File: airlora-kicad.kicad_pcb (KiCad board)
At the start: 4 copper layers, 77 x 77 mm, 185 parts, among them IC1 BALFHB-WL-02D3, J1 12V, J10 I2C, J11 UART2, J12 UART_MAIN, J2 Conn_Coaxial, J3 Led, J4 SHT, J5 I2C, J6 A_NO2, J7 UART1, J8 A_CO, J9 I2C, Q1 S8050, Q2 S8050, Q3 S8050, Q4 S8050, Q5 S8050, Q6 S8050, Q7 S8050, Q8 S8050, Q9 S8050, SW1 SW_Push, SW2 SW_Slide_DPDT, SW3 SW_Push, U1 TPS7A2633DRVR, U2 TPS54202DDC, U3 TPS7A2633DRVR, U4 BGS12WN6E6327, U5 STM32WLE5CCUx, U6 STM32F103C8Tx, X1 32MHZ, Y1 32.768kHz, Y2 8Mhz

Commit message: Update PCB layout
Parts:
- removed C10, C9: 1uF, Capacitor_SMD:C_0805_2012Metric
- removed C42: 4.7uF, Capacitor_SMD:C_0603_1608Metric
- removed C43, C44, C45, C46, C47: 100nf, Capacitor_SMD:C_0402_1005Metric
- removed C48, C49: 22PF, Capacitor_SMD:C_0402_1005Metric
- removed C50: 100nF, Capacitor_SMD:C_0402_1005Metric
- removed D4: LED, LED_SMD:LED_0603_1608Metric_Pad1.05x0.95mm_HandSolder
- removed J6: A_NO2, Connector_JST:JST_XH_B3B-XH-A_1x03_P2.50mm_Vertical
- removed J8: A_CO, Connector_JST:JST_XH_B3B-XH-A_1x03_P2.50mm_Vertical
- removed Q5, Q7: S8050, Package_TO_SOT_SMD:SOT-23
- removed R28, R29: 10k, Resistor_SMD:R_0402_1005Metric
- removed SW2: SW_Slide_DPDT, Button_Switch_THT:SW_E-Switch_EG1271_SPDT
- removed SW3: SW_Push, Button_Switch_SMD:SW_Tactile_SPST_NO_Straight_CK_PTS636Sx25SMTRLFS
- removed U3: TPS7A2633DRVR, footprint:TPS7A2633DRVR
- removed U6: STM32F103C8Tx, Package_QFP:LQFP-48_7x7mm_P0.5mm
- removed X1: 32MHZ, footprint:NX2016SA_NDK
- removed Y2: 8Mhz, Crystal:Crystal_SMD_3225-4Pin_3.2x2.5mm
- removed kibuzzard-667528BC: G***, kibuzzard-667528BC
- removed kibuzzard-667528D4: G***, kibuzzard-667528D4
- removed the kibuzzard-66752922 at (124.1, 87.6)
- removed the kibuzzard-66752922 at (123.9, 76.0)
- removed the kibuzzard-667540EB at (124.1, 85.1)
- removed the kibuzzard-667540EB at (123.9, 73.6)
- removed kibuzzard-66754104: G***, kibuzzard-66754104
- removed the kibuzzard-66754176 at (96.7, 89.6)
- removed kibuzzard-667541E6 (x4): G***, kibuzzard-667541E6
- removed kibuzzard-667541EF (x4): G***, kibuzzard-667541EF
- removed kibuzzard-66754524: G***, kibuzzard-66754524
- removed the kibuzzard-66763ACD at (81.7, 87.9)
- removed kibuzzard-668CA440: G***, kibuzzard-668CA440
- removed kibuzzard-668CA458: G***, kibuzzard-668CA458
- removed kibuzzard-668CA46A: G***, kibuzzard-668CA46A
- removed kibuzzard-668CA479: G***, kibuzzard-668CA479
- removed kibuzzard-668CA498: G***, kibuzzard-668CA498
- removed kibuzzard-668CA4A7: G***, kibuzzard-668CA4A7
- removed kibuzzard-668CA4B6: G***, kibuzzard-668CA4B6
- removed kibuzzard-668CA4DF: G***, kibuzzard-668CA4DF
- removed kibuzzard-668CA658: G***, kibuzzard-668CA658
- removed kibuzzard-668CA679: G***, kibuzzard-668CA679
- removed kibuzzard-668F38B2: G***, kibuzzard-668F38B2
- removed kibuzzard-6690D059: G***, kibuzzard-6690D059
- removed kibuzzard-6690D084: G***, kibuzzard-6690D084
- removed kibuzzard-6690D099: G***, kibuzzard-6690D099
- added J13: UART_MAIN, Connector_JST:JST_XH_B3B-XH-A_1x03_P2.50mm_Vertical, F.Cu at (183.6, 86.8)
- added J14: Conn_01x02_Pin, Connector_PinHeader_2.54mm:PinHeader_1x02_P2.54mm_Vertical, F.Cu at (129.7, 96.8)
- added J15: Conn_01x02_Pin, Connector_PinHeader_2.54mm:PinHeader_1x02_P2.54mm_Vertical, F.Cu at (142.8, 90.9)
- added L6: 1400R@1GHz, Inductor_SMD:L_0402_1005Metric, F.Cu at (172.4, 103.3)
- added TP1: TestPoint, TestPoint:TestPoint_Loop_D1.80mm_Drill1.0mm_Beaded, F.Cu at (134.5, 76.2)
- added TP2: TestPoint, TestPoint:TestPoint_Loop_D1.80mm_Drill1.0mm_Beaded, F.Cu at (138.6, 76.2)
- added TP3: TestPoint, TestPoint:TestPoint_Loop_D1.80mm_Drill1.0mm_Beaded, F.Cu at (149.0, 103.8)
- added TP4: TestPoint, TestPoint:TestPoint_Loop_D1.80mm_Drill1.0mm_Beaded, F.Cu at (144.2, 103.8)
- added TP5: TestPoint, TestPoint:TestPoint_Loop_D1.80mm_Drill1.0mm_Beaded, F.Cu at (165.6, 80.7)
- added TP6: TestPoint, TestPoint:TestPoint_Loop_D1.80mm_Drill1.0mm_Beaded, F.Cu at (169.9, 80.7)
- added XTAL1: NT2016SA-32M-END4263A, footprint:NT2016SA-32M-END4263A_NDK, F.Cu at (171.8, 105.9)
- added kibuzzard-66752922: G***, kibuzzard-66752922, F.Cu at (175.7, 92.1)
- added kibuzzard-66A47256: G***, kibuzzard-66A47256, F.Cu at (122.2, 115.1)
- added kibuzzard-66A70081: G***, kibuzzard-66A70081, B.Cu at (145.7, 63.9)
- added kibuzzard-66A7008A: G***, kibuzzard-66A7008A, B.Cu at (147.7, 63.9)
- added kibuzzard-66A70091: G***, kibuzzard-66A70091, B.Cu at (159.5, 64.0)
- added kibuzzard-66A70098: G***, kibuzzard-66A70098, B.Cu at (161.4, 64.0)
- added kibuzzard-66A700A1: G***, kibuzzard-66A700A1, B.Cu at (173.2, 64.1)
- added kibuzzard-66A704F7: G***, kibuzzard-66A704F7, B.Cu at (175.2, 64.1)
- added kibuzzard-66A704FE: G***, kibuzzard-66A704FE, F.Cu at (170.5, 84.8)
- added kibuzzard-66A704FE: G***, kibuzzard-66A704FE, B.Cu at (179.6, 75.3)
- added kibuzzard-66A70504: G***, kibuzzard-66A70504, F.Cu at (165.2, 84.8)
- added kibuzzard-66A70504: G***, kibuzzard-66A70504, B.Cu at (179.6, 72.8)
- added kibuzzard-66A7052C: G***, kibuzzard-66A7052C, F.Cu at (132.4, 80.3)
- added kibuzzard-66A70534: G***, kibuzzard-66A70534, F.Cu at (140.5, 80.3)
- added kibuzzard-66A705CB: G***, kibuzzard-66A705CB, F.Cu at (149.4, 108.3)
- added kibuzzard-66A705D3: G***, kibuzzard-66A705D3, F.Cu at (144.1, 108.3)
- added kibuzzard-66A7121E: G***, kibuzzard-66A7121E, F.Cu at (175.7, 86.9)
- added kibuzzard-66A71226: G***, kibuzzard-66A71226, F.Cu at (175.7, 89.5)
- added kibuzzard-66A7130C: G***, kibuzzard-66A7130C, F.Cu at (146.5, 113.3)
- added kibuzzard-66A71314: G***, kibuzzard-66A71314, F.Cu at (151.3, 113.3)
- added kibuzzard-66A71938: G***, kibuzzard-66A71938, F.Cu at (148.3, 75.3)
- C3: footprint Capacitor_SMD:C_0402_1005Metric -> Capacitor_SMD:C_0603_1608Metric
- C37, C41: value 6.8pF -> 10pF
- J11: value UART2 -> Conn_01x02_Pin; footprint Connector_JST:JST_XH_B4B-XH-A_1x04_P2.50mm_Vertical -> Connector_PinHeader_2.54mm:PinHeader_1x02_P2.54mm_Vertical
- J12: value UART_MAIN -> STlink; footprint Connector_JST:JST_XH_B4B-XH-A_1x04_P2.50mm_Vertical -> Connector_JST:JST_XH_B5B-XH-A_1x05_P2.50mm_Vertical
- R10: value 10K -> 220
- R11: value 1.96M -> 3k
- R12: value 1.18M -> 1K; footprint Resistor_SMD:R_0402_1005Metric -> Resistor_SMD:R_0603_1608Metric
- R13: value 1k -> 1K; footprint Resistor_SMD:R_0402_1005Metric -> Resistor_SMD:R_0603_1608Metric
- R16, R22, R24: value 1K -> 4.7K
- R27: value 1k -> 4.7K
- moved J12 119.0 mm to (183.6, 100.2)
- moved kibuzzard-6690D08F 107.0 mm to (176.9, 110.4)
- moved R10 91.3 mm to (169.5, 104.5)
- moved R12 76.9 mm to (151.5, 122.3)
- moved R13 70.6 mm to (146.4, 122.3)
- moved R27 70.4 mm to (149.1, 101.3), turned to 0 degrees
- moved C33 69.6 mm to (165.8, 93.6), turned to 180 degrees
- moved C36 68.2 mm to (163.9, 93.6), turned to 180 degrees
- moved C6 68.0 mm to (135.4, 88.5)
- moved U1 68.0 mm to (135.4, 91.2)
- moved C1 68.0 mm to (135.6, 93.8)
- moved R2 68.0 mm to (131.4, 92.0)
- moved R3 68.0 mm to (131.4, 90.5)
- moved R4 68.0 mm to (131.4, 89.0)
- moved Y1 67.1 mm to (164.8, 95.0), turned to 0 degrees
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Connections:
- C29 pad 2: /AirLora V3/MCU/RFO_LP -> /AirLora V3/MCU/RFO_HP
- C37 pad 1: GND -> Net-(XTAL1-VCC)
- C37 pad 2: Net-(U5-OSC_IN) -> GND
- C41 pad 1: Net-(U5-OSC_OUT) -> /AirLora V3/MCU/XTA
- C41 pad 2: GND -> Net-(C41-Pad2)
- C6 pad 1: +3.3V_HP -> Net-(J15-Pin_1)
- C7 pad 1: +5V -> a
- C8 pad 1: +5V -> a
- D1 pad 2: +3.3V_HP -> +3.3V
- D3 pad 2: +3.3V -> +12V
- J1 pad 1: +12V -> Net-(J1-Pin_1)
- J10 pad 3: /AirLora V3/MCU Sub/SCL1 -> /AirLora V3/MCU/SCL2
- J10 pad 4: /AirLora V3/MCU Sub/SDA1 -> /AirLora V3/MCU/SDA2
- J11 pad 1: GND -> Net-(J1-Pin_1)
- J11 pad 2: +3.3V -> +12V
- J12 pad 1: /AirLora V3/MCU/UART1_RX -> +3.3V
- J12 pad 2: /AirLora V3/MCU/UART1_TX -> GND
- J12 pad 3: /AirLora V3/MCU/NRST -> /AirLora V3/MCU/T_SWDIO
- J12 pad 4: GND -> /AirLora V3/MCU/T_SWCLK
- J4 pad 3: /AirLora V3/MCU Sub/SCL1 -> /AirLora V3/MCU/SCL2
- J4 pad 4: /AirLora V3/MCU Sub/SDA1 -> /AirLora V3/MCU/SDA2
- J5 pad 3: /AirLora V3/MCU Sub/SCL1 -> /AirLora V3/MCU/SCL2
- J5 pad 4: /AirLora V3/MCU Sub/SDA1 -> /AirLora V3/MCU/SDA2
- J7 pad 3: /AirLora V3/MCU Sub/TX3 -> /AirLora V3/MCU/UART1_TX
- J7 pad 4: /AirLora V3/MCU Sub/RX3 -> /AirLora V3/MCU/UART1_RX
- J9 pad 3: /AirLora V3/MCU Sub/SCL1 -> /AirLora V3/MCU/SCL2
- J9 pad 4: /AirLora V3/MCU Sub/SDA1 -> /AirLora V3/MCU/SDA2
- L1 pad 2: +5V -> a
- L5 pad 2: /AirLora V3/MCU/RFO_LP -> /AirLora V3/MCU/RFO_HP
- Q1 pad 2: Net-(J3-Pin_2) -> Net-(Q1-E)
- Q2 pad 2: Net-(J3-Pin_1) -> Net-(Q2-E)
- R1 pad 2: /AirLora V3/MCU/PA3 -> /AirLora V3/Power/En
- R10 pad 2: +3.3V -> Net-(C41-Pad2)
- R11 pad 1: +3.3V -> Net-(D3-K)
- R11 pad 2: Net-(U3-NC) -> GND
- R12 pad 1: Net-(U3-NC) -> Net-(Q2-E)
- R12 pad 2: GND -> Net-(J3-Pin_1)
- R13 pad 1: Net-(D3-K) -> Net-(Q1-E)
- R13 pad 2: GND -> Net-(J3-Pin_2)
- R16 pad 1: Net-(U5-PA4) -> /AirLora V3/MCU/SDA2
- R16 pad 2: /AirLora V3/MCU Sub/PA8 -> +3.3V
- R18 pad 1: /AirLora V3/MCU/PA5 -> /AirLora V3/MCU/PB8
- R19 pad 1: /AirLora V3/MCU/PA6 -> /AirLora V3/MCU/PA0
- R2 pad 2: +3.3V_HP -> Net-(J15-Pin_1)
- R20 pad 1: /AirLora V3/MCU Sub/PA15 -> /AirLora V3/MCU/PB3
- R21 pad 2: /AirLora V3/MCU Sub/PA7 -> /AirLora V3/MCU/PB3
- R22 pad 1: /AirLora V3/MCU Sub/PA6 -> /AirLora V3/MCU/SCL2
- R22 pad 2: Net-(Q5-B) -> +3.3V
- R23 pad 1: /AirLora V3/MCU Sub/PA5 -> /AirLora V3/MCU/PB3
- R24 pad 1: /AirLora V3/MCU Sub/PA4 -> /AirLora V3/MCU/SDA3
- R24 pad 2: Net-(Q7-B) -> +3.3V
- R25 pad 1: /AirLora V3/MCU Sub/PB3 -> /AirLora V3/MCU/PB3
- R26 pad 1: /AirLora V3/MCU Sub/PB4 -> /AirLora V3/MCU/PB3
- R27 pad 1: Net-(D4-K) -> /AirLora V3/MCU/SCL3
- R27 pad 2: GND -> +3.3V
- R3 pad 1: +3.3V_HP -> Net-(J15-Pin_1)
- R7 pad 2: +5V -> a
- U1 pad 1: +3.3V_HP -> Net-(J15-Pin_1)
- U5 pad 1: unconnected-(U5-PB3-Pad1) -> /AirLora V3/MCU/PB3
- U5 pad 10: /AirLora V3/MCU/PA3 -> /AirLora V3/MCU/UART2_RX
- U5 pad 12: Net-(U5-PA4) -> unconnected-(U5-PA4-Pad12)
- U5 pad 13: /AirLora V3/MCU/PA5 -> /AirLora V3/MCU/FE_CTRL1
- U5 pad 14: /AirLora V3/MCU/PA6 -> unconnected-(U5-PA6-Pad14)
- U5 pad 15: unconnected-(U5-PA7-Pad15) -> /AirLora V3/MCU/SCL3
- U5 pad 2: unconnected-(U5-PB4-Pad2) -> /AirLora V3/MCU/SDA3
- U5 pad 22: /AirLora V3/MCU/RFO_LP -> unconnected-(U5-RFO_LP-Pad22)
- U5 pad 23: unconnected-(U5-RFO_HP-Pad23) -> /AirLora V3/MCU/RFO_HP
- U5 pad 26: Net-(U5-OSC_IN) -> /AirLora V3/MCU/XTA
- U5 pad 27: Net-(U5-OSC_OUT) -> unconnected-(U5-OSC_OUT-Pad27)
- U5 pad 30: unconnected-(U5-PB0-VDD_TCXO-Pad30) -> /AirLora V3/MCU/PB0
- U5 pad 34: /AirLora V3/MCU Sub/SCL2 -> /AirLora V3/MCU/SDA2
- U5 pad 35: /AirLora V3/MCU Sub/SDA2 -> /AirLora V3/MCU/SCL2
- U5 pad 38: /AirLora V3/MCU/FE_CTRL1 -> unconnected-(U5-PC13-Pad38)
- U5 pad 6: unconnected-(U5-PB8-Pad6) -> /AirLora V3/MCU/PB8
- U5 pad 7: unconnected-(U5-PA0-Pad7) -> /AirLora V3/MCU/PA0
- U5 pad 9: unconnected-(U5-PA2-Pad9) -> /AirLora V3/MCU/UART2_TX
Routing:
- net /AirLora V3/MCU/PB3: track 0.00 -> 97.3 mm, vias 0 -> 4
- net /AirLora V3/MCU/SDA2: track 0.00 -> 81.1 mm, vias 0 -> 5
- net /AirLora V3/MCU/SCL2: track 0.00 -> 79.4 mm, vias 0 -> 5
- net /AirLora V3/MCU Sub/SDA1: track 62.6 -> 0.00 mm, vias 4 -> 0
- net /AirLora V3/MCU Sub/SCL1: track 60.4 -> 0.00 mm, vias 4 -> 0
- net /AirLora V3/MCU/NRST: track 114.6 -> 54.3 mm
- net +5V: track 169.6 -> 111.0 mm, vias 5 -> 2
- net /AirLora V3/MCU/PA3: track 51.9 -> 0.00 mm, vias 2 -> 0
- net /AirLora V3/MCU Sub/TX3: track 51.8 -> 0.00 mm, vias 2 -> 0
- net /AirLora V3/MCU Sub/RX3: track 48.9 -> 0.00 mm, vias 2 -> 0
- net /AirLora V3/MCU/UART2_RX: track 0.00 -> 48.3 mm, vias 0 -> 1
- net /AirLora V3/MCU/UART2_TX: track 0.00 -> 46.5 mm, vias 0 -> 1
- net /AirLora V3/MCU/PA5: track 46.1 -> 0.00 mm, vias 2 -> 0
- net Net-(U5-PA4): track 44.3 -> 0.00 mm, vias 3 -> 0
- net /AirLora V3/MCU/PA6: track 42.7 -> 0.00 mm, vias 2 -> 0
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- added copper zone on F.Cu, net Net-(J15-Pin_1)
- added copper zone on F.Cu, net a
- removed copper zone on F.Cu, net +3.3V_HP
- removed copper zone on In2.Cu, net +3.3V_HP

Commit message: Update PCB layout
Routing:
- net GND: vias 91 -> 366

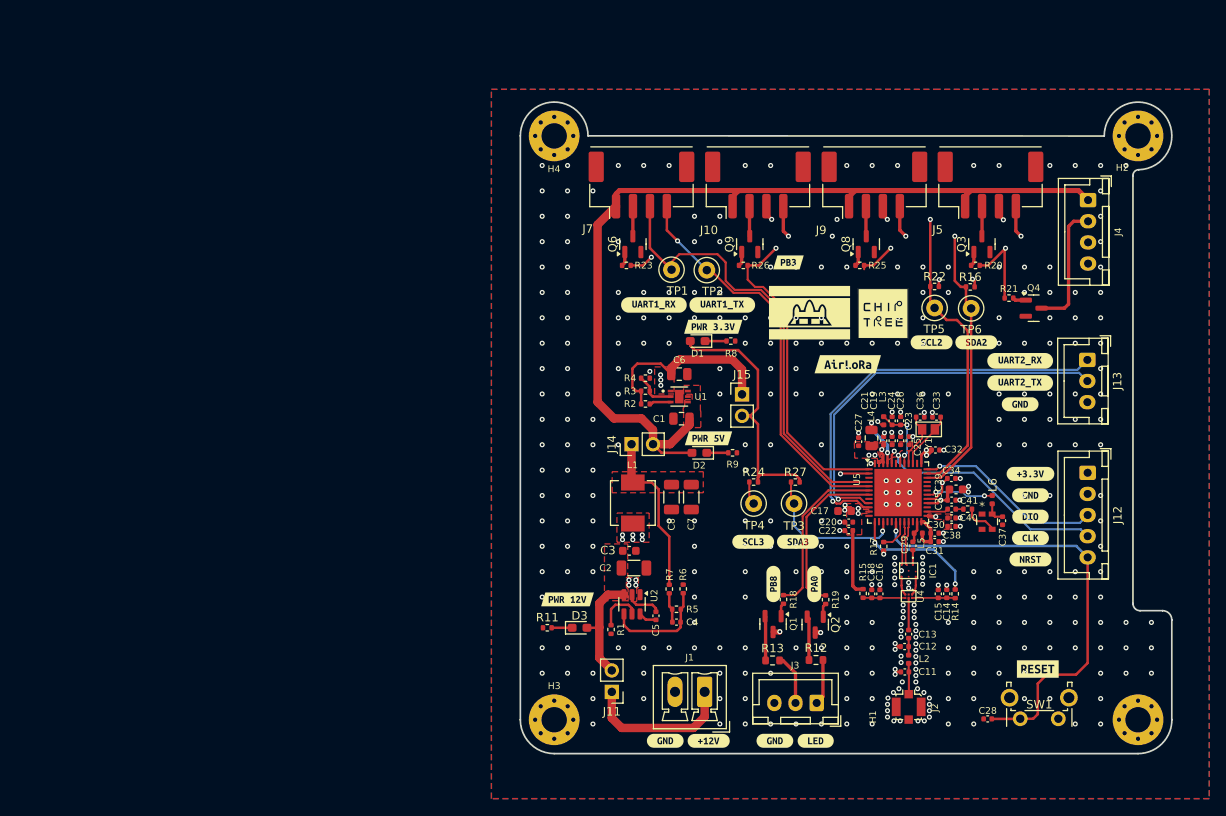
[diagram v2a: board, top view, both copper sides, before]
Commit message: Update antenna
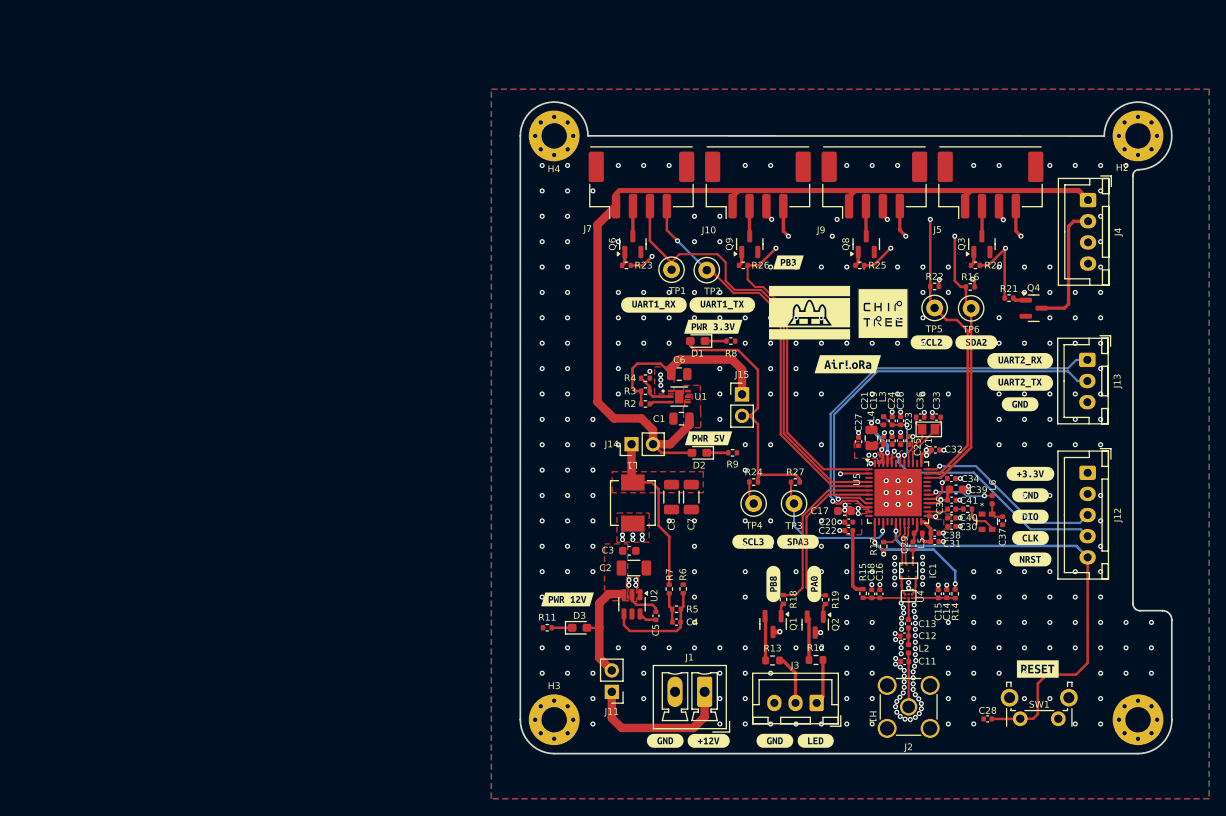
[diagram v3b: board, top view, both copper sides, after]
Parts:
- removed R1: 1k, Resistor_SMD:R_0402_1005Metric
- J2: footprint Connector_Coaxial:U.FL_Molex_MCRF_73412-0110_Vertical -> Connector_Coaxial:SMA_Amphenol_132134-11_Vertical
- moved C11 1.23 mm to (162.0, 122.5)
- moved C12 1.23 mm to (162.0, 119.5)
- moved C13 1.23 mm to (162.5, 118.0)
- moved L2 1.23 mm to (162.5, 121.0)
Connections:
- net a renamed /AirLora V3/Power/SW
- U2 pad 5: Net-(U2-EN) -> unconnected-(U2-EN-Pad5)
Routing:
- net Net-(U2-EN): track 5.55 -> 0.00 mm
- net GND: track 17.1 -> 13.9 mm, vias 366 -> 371
- net Net-(J2-In): track 3.50 -> 6.39 mm
- net Net-(U4-RFIN): track 3.82 -> 2.60 mm
